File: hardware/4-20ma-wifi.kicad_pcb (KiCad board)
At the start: 2 copper layers, 46 x 82 mm, 36 parts, among them J1 Conn_01x19_Female, J2 Conn_01x19_Female, J3 Screw_Terminal_01x02, J4 Screw_Terminal_01x02, J5 Screw_Terminal_01x02, J6 Screw_Terminal_01x02, K1 G5V-1, K2 G5V-1, M1 DC-DC_Buck_Step_Module-dc-dc_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, Q1 2N7002E, Q2 2N7002E, SW1 SW_DIP_x01, U2 LMP8640

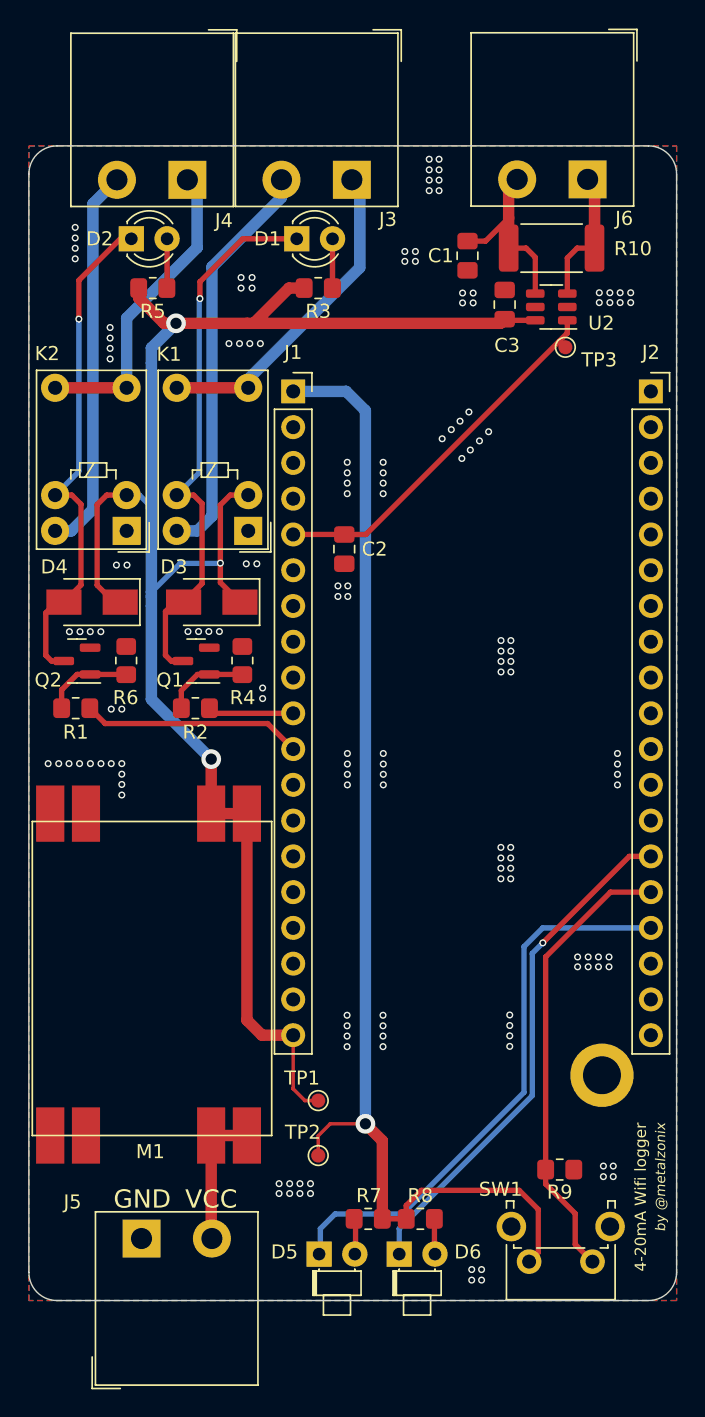
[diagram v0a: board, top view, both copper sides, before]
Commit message: Work around PCB design. Added ADC121 to the schematic
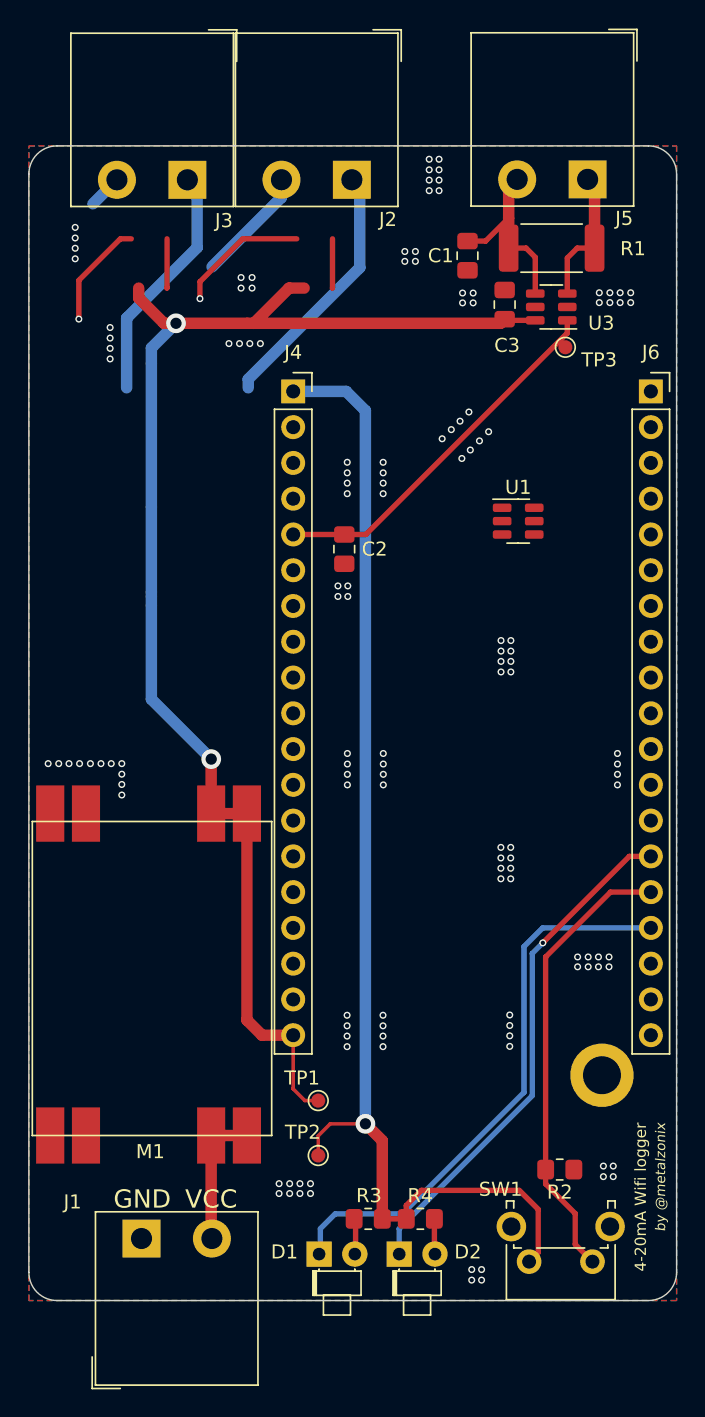
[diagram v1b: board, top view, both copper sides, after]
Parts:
- removed the D1 at (157.0, 47.6)
- removed the D2 at (145.3, 47.6)
- removed D3, D4: 1N4004, Diode_SMD:D_SMA
- removed K1, K2: G5V-1, Relay_THT:Relay_SPDT_Omron_G5V-1
- removed Q1, Q2: 2N7002E, Package_TO_SOT_SMD:SOT-23
- removed the R1 at (141.3, 80.9)
- removed the R2 at (149.8, 80.9)
- removed the R3 at (158.6, 51.1)
- removed the R4 at (153.2, 77.6)
- removed R5: 1k, Resistor_SMD:R_0805_2012Metric_Pad1.20x1.40mm_HandSolder
- removed R6: 10k, Resistor_SMD:R_0805_2012Metric_Pad1.20x1.40mm_HandSolder
- added U1: ADC121C027CIMK, Package_TO_SOT_SMD:SOT-23-6, F.Cu at (172.8, 67.7)
- renumbered D5 to D1, D6 to D2, J5 to J1, J3 to J2, J4 to J3, J1 to J4, J6 to J5, J2 to J6, R10 to R1, R9 to R2, R7 to R3, R8 to R4, U2 to U3
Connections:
- C2 pad 1: vsens -> Net-(C2-Pad1)
- J2 pad 1: Net-(J3-Pad1) -> unconnected-(J2-Pad1)
- J2 pad 2: Net-(J3-Pad2) -> unconnected-(J2-Pad2)
- J3 pad 1: Net-(J4-Pad1) -> unconnected-(J3-Pad1)
- J3 pad 2: Net-(J4-Pad2) -> unconnected-(J3-Pad2)
- J4 pad 10: relay1 -> unconnected-(J4-Pad10)
- J4 pad 11: relay2 -> unconnected-(J4-Pad11)
- J4 pad 5: vsens -> adc_uc
- J6 pad 3: unconnected-(J2-Pad3) -> scl
- J6 pad 6: unconnected-(J2-Pad6) -> sda
- U3 pad 1: vsens -> Net-(C2-Pad1)
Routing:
- net Net-(D1-Pad1): track 39.0 -> 0.00 mm, vias 1 -> 0
- net Net-(D2-Pad1): track 36.5 -> 0.00 mm, vias 1 -> 0
- net Net-(J3-Pad2): track 28.9 -> 0.00 mm
- net +5V: track 126.4 -> 98.6 mm, vias 3 -> 2
- net Net-(J4-Pad2): track 27.4 -> 0.00 mm
- net vsens: track 26.9 -> 0.00 mm
- net Net-(C2-Pad1): track 0.00 -> 26.9 mm
- net Net-(J3-Pad1): track 23.4 -> 0.00 mm
- net Net-(J4-Pad1): track 22.2 -> 0.00 mm
- net unconnected-(J2-Pad1): track 0.00 -> 18.3 mm
- net unconnected-(J3-Pad1): track 0.00 -> 17.1 mm
- net (no net): track 0.00 -> 17.0 mm, vias 0 -> 2
- net relay2: track 15.6 -> 0.00 mm
- net unconnected-(J2-Pad2): track 0.00 -> 8.23 mm
- net Net-(Q2-Pad1): track 6.35 -> 0.00 mm
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
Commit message: Work around PCB design
- Added new terminal block to connect usar or i2c device
- Added shift-level to 3.3 - 5v usart/i2c
- Work around layout
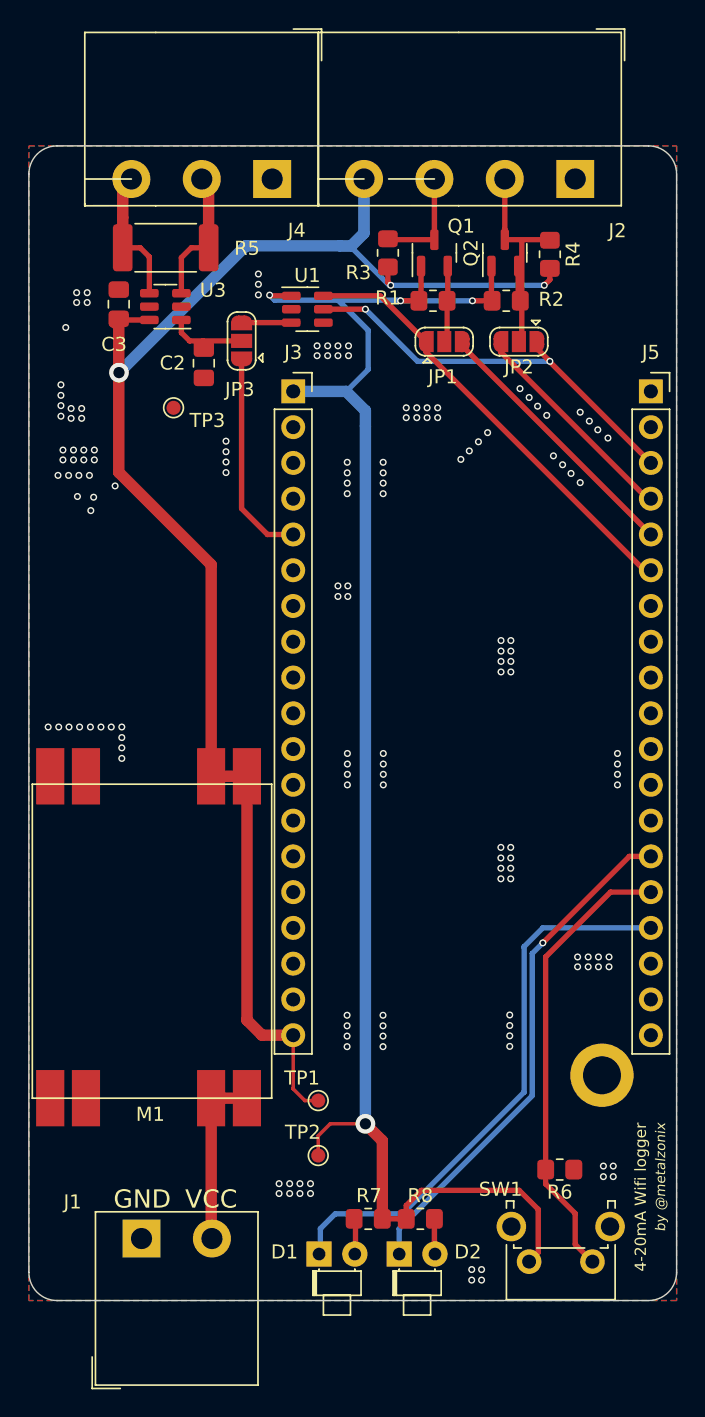
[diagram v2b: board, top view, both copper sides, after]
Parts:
- removed C1: 10 uF, Capacitor_SMD:C_0805_2012Metric_Pad1.18x1.45mm_HandSolder
- removed the J3 at (149.3, 43.4)
- removed J6: Conn_01x19_Female, Connector_PinSocket_2.54mm:PinSocket_1x19_P2.54mm_Vertical
- added J5: Conn_01x19_Female, Connector_PinSocket_2.54mm:PinSocket_1x19_P2.54mm_Vertical, F.Cu at (182.2, 58.4)
- added JP1: SolderJumper_3_Open, Jumper:SolderJumper-3_P1.3mm_Open_RoundedPad1.0x1.5mm, F.Cu at (167.5, 54.9)
- added JP2: SolderJumper_3_Open, Jumper:SolderJumper-3_P1.3mm_Open_RoundedPad1.0x1.5mm, F.Cu at (172.8, 54.9)
- added JP3: SolderJumper_3_Open, Jumper:SolderJumper-3_P1.3mm_Open_RoundedPad1.0x1.5mm, F.Cu at (153.1, 54.9)
- added Q1: BSS138, Package_TO_SOT_SMD:SOT-23, F.Cu at (166.8, 48.6)
- added Q2: BSS138, Package_TO_SOT_SMD:SOT-23, F.Cu at (171.8, 48.6)
- added R1: 10k, Resistor_SMD:R_0805_2012Metric_Pad1.20x1.40mm_HandSolder, F.Cu at (166.7, 52.0)
- added R2: 10k, Resistor_SMD:R_0805_2012Metric_Pad1.20x1.40mm_HandSolder, F.Cu at (171.9, 52.0)
- added R3: 10k, Resistor_SMD:R_0805_2012Metric_Pad1.20x1.40mm_HandSolder, F.Cu at (163.5, 48.6)
- added R4: 10k, Resistor_SMD:R_0805_2012Metric_Pad1.20x1.40mm_HandSolder, F.Cu at (175.0, 48.7)
- J2: value Screw_Terminal_01x02 -> Screw_Terminal_01x04; footprint project_library:TerminalBlock__1x02_P5.00mm_90Degree -> project_library:TerminalBlock__1x04_P5.00mm_90Degree
- J4: renamed from J5; value Screw_Terminal_01x02 -> Screw_Terminal_01x03; footprint project_library:TerminalBlock__1x02_P5.00mm_90Degree -> project_library:TerminalBlock__1x03_P5.00mm_90Degree
- moved TP3 28.2 mm to (148.3, 59.6)
- moved C3 27.4 mm to (144.4, 52.2)
- moved R5 27.4 mm to (147.7, 48.2)
- moved U3 27.4 mm to (147.7, 52.4)
- moved J4 22.4 mm to (155.3, 43.4)
- moved U1 21.2 mm to (157.8, 52.6)
- moved C2 16.5 mm to (150.4, 56.4)
- moved J2 15.9 mm to (176.8, 43.4)
- moved M1 2.65 mm to (138.2, 108.6)
- renumbered J4 to J3, R1 to R5, R2 to R6, R3 to R7, R4 to R8
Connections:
- J1 pad 2: Net-(J1-Pad2) -> +12V
- J2 pad 1: unconnected-(J2-Pad1) -> GND
- J2 pad 2: unconnected-(J2-Pad2) -> Net-(J2-Pad2)
- J4 pad 1: Net-(J5-Pad1) -> +12V
- J4 pad 2: Net-(C1-Pad1) -> Net-(J4-Pad2)
- M1 pad 1: Net-(J1-Pad2) -> +12V
- R5 pad 1: Net-(J5-Pad1) -> Net-(J4-Pad2)
- R5 pad 2: Net-(C1-Pad1) -> GND
- U1 pad 4: unconnected-(U1-Pad4) -> GND
- U3 pad 3: Net-(J5-Pad1) -> Net-(J4-Pad2)
- U3 pad 4: Net-(C1-Pad1) -> GND
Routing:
- net +3V3: track 85.7 -> 117.8 mm, vias 1 -> 4
- net sda: track 0.00 -> 31.8 mm
- net scl: track 0.00 -> 30.1 mm, vias 0 -> 2
- net Net-(C2-Pad1): track 26.9 -> 6.00 mm
- net rx: track 0.00 -> 19.2 mm
- net unconnected-(J2-Pad1): track 18.3 -> 0.00 mm
- net unconnected-(J3-Pad1): track 17.1 -> 0.00 mm
- net (no net): track 17.0 -> 0.00 mm, vias 2 -> 0
- net Net-(J2-Pad2): track 0.00 -> 16.8 mm
- net tx: track 0.00 -> 15.7 mm
- net adc_uc: track 0.00 -> 15.0 mm
- net Net-(C1-Pad1): track 13.6 -> 0.00 mm
- net +5V: track 98.6 -> 111.1 mm, vias 2 -> 3
- net +12V: track 0.00 -> 12.5 mm
- net GND: track 0.00 -> 10.0 mm, vias 135 -> 155
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
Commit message: Work around pcb layout
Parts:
- removed TP3: TestPoint, TestPoint:TestPoint_Pad_D1.0mm
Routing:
- net +12V: track 12.5 -> 89.5 mm
- net Net-(J2-Pad2): track 16.8 -> 7.70 mm
- net Net-(JP2-Pad2): track 0.00 -> 5.47 mm
- net +3V3: track 117.8 -> 121.3 mm
- net GND: track 10.0 -> 11.5 mm, vias 155 -> 138
- net +5V: track 111.1 -> 111.6 mm, vias 3 -> 5
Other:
- board text added: "Granja Zero Waste"
- board text added: "by libertas inves"
- board text removed: "4-20mA Wifi logger"
- board text removed: "by @metalzonix"

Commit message: Added LP2980 Dropout regulator to power the ADC converter
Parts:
- added C1: 100 nF, Capacitor_SMD:C_0805_2012Metric_Pad1.18x1.45mm_HandSolder, F.Cu at (160.4, 51.6)
- added C2: C_Polarized_US, Capacitor_Tantalum_SMD:CP_EIA-3216-18_Kemet-A, F.Cu at (158.0, 49.3)
- added U1: LP2980-ADJ, Package_TO_SOT_SMD:SOT-23-5, F.Cu at (156.0, 52.5)
- moved U2 3.50 mm to (160.5, 54.8)
- moved JP3 1.87 mm to (152.6, 56.6)
- moved R5 1.16 mm to (147.7, 49.4)
- moved C4 1.16 mm to (144.4, 53.4)
- moved JP1 1.16 mm to (167.5, 56.1)
- moved JP2 1.16 mm to (172.8, 56.1)
- moved Q1 1.16 mm to (166.8, 49.8)
- moved Q2 1.16 mm to (171.8, 49.8)
- moved R1 1.16 mm to (166.7, 53.2)
- moved R2 1.16 mm to (171.9, 53.2)
- moved R3 1.16 mm to (163.5, 49.8)
- moved R4 1.16 mm to (175.0, 49.9)
- moved U4 1.16 mm to (147.7, 53.6)
- moved J2 1.15 mm to (176.8, 44.5)
- moved J4 1.15 mm to (155.3, 44.5)
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- renumbered C2 to C3, C3 to C4, U1 to U2, U3 to U4
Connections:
- U2 pad 1: +3V3 -> Net-(C1-Pad1)
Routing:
- net +12V: track 89.5 -> 97.3 mm
- net Net-(C1-Pad1): track 0.00 -> 6.78 mm
- net +5V: track 111.6 -> 117.9 mm, vias 5 -> 4
- net +3V3: track 121.3 -> 115.0 mm, vias 4 -> 3
- net scl: track 30.3 -> 26.4 mm
- net adc121: track 3.53 -> 6.93 mm
- net sda: track 31.8 -> 28.4 mm
- net Net-(C3-Pad1): track 6.00 -> 4.31 mm
- net GND: track 11.5 -> 10.0 mm, vias 138 -> 140

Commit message: Minor changes - prepare release
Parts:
- added JP3: SolderJumper_2_Open, Jumper:SolderJumper-2_P1.3mm_Open_Pad1.0x1.5mm, F.Cu at (142.4, 49.4)
- C2: value C_Polarized_US -> 4.7 uF
- renumbered JP3 to JP4
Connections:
- J4 pad 3: GND -> Net-(J4-Pad3)
- R5 pad 2: GND -> Net-(J4-Pad3)
- U4 pad 4: GND -> Net-(J4-Pad3)
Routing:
- net Net-(J4-Pad3): track 0.00 -> 12.8 mm
- net GND: track 10.0 -> 0.00 mm, vias 140 -> 138
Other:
- board text added: "by re2v"
- board text removed: "by libertas inves"
